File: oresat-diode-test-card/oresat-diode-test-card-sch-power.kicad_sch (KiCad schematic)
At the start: 90 parts, among them Q1 DMP2240UDM, Q2 DMP3050LVT-7, Q7 MOSFET-PCH-SOT23-6, Q8 PMV45EN, Q9 PMV45EN, U10 TPS62111RSA, U11 MIC842LYC5, U12 MIC842LYC5, U2 MAX7310, U3 TS5A21366DCUR, U6 MAX4211

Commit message: Quick design review on schematic; basically ready for layout.
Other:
- title: OreSat M0 Proto Card: Power -> OreSat Diode Test Card
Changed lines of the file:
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@@
 	(paper "USLedger")
 	(title_block
-		(title "OreSat M0 Proto Card: Power")
-		(date "2024-03-21")
-		(rev "5.0")
+		(title "OreSat Diode Test Card")
+		(date "2024-04-21")
+		(rev "v1.0")
 	)
 	(junction

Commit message: Lots of schematic cleanup - replace weird ground and power symbols with more kicad ones, fix values, fix OPD connections and address, update PCB
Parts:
- removed R6, R7: 0, oresat-passives:0603-C-NOSILK, symbol oresat-proto-card-eagle-import:R-US_0603-C-NOSILK
- added TP301: TEST-POINT-LARGE-SQUARE, oresat-proto-card:1X01, symbol oresat-proto-card-eagle-import:TEST-POINT-LARGE-SQUARE
- R1, R2: value RC0603FR-0710KL -> 2.7k
- R17: value 10k -> 2.7k
- R3: value 2.7k -> 10k
- R46, R54, R58: value NP -> 2.7k; now fitted
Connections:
- net CB_CTRL is gone; now on net CB-RESET: Q9.1 (G), R5.1, TP39.1, U6.3 (LE), U6.4 (COUT1), U6.6 (COUT2)
- net at U2.5 (IO1): now also TP301.1
- net UART_EN: now reaches U3.3 (IN2), U3.7 (IN1)
- net UART_EN: now also U2.12 (IO7)
- net at TP36.1: now also U2.4 (IO0); no longer U2.12 (IO7)
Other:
- note added: "Address selection for Card (See MAX7310 datasheet) OreSat Diode Test Card = 0x11"
- note removed: "Address selection for Card (See MAX7310 datasheet)"
- note removed: "To STM32 I2C bootloader"
- moved on the sheet: TP36, TP40

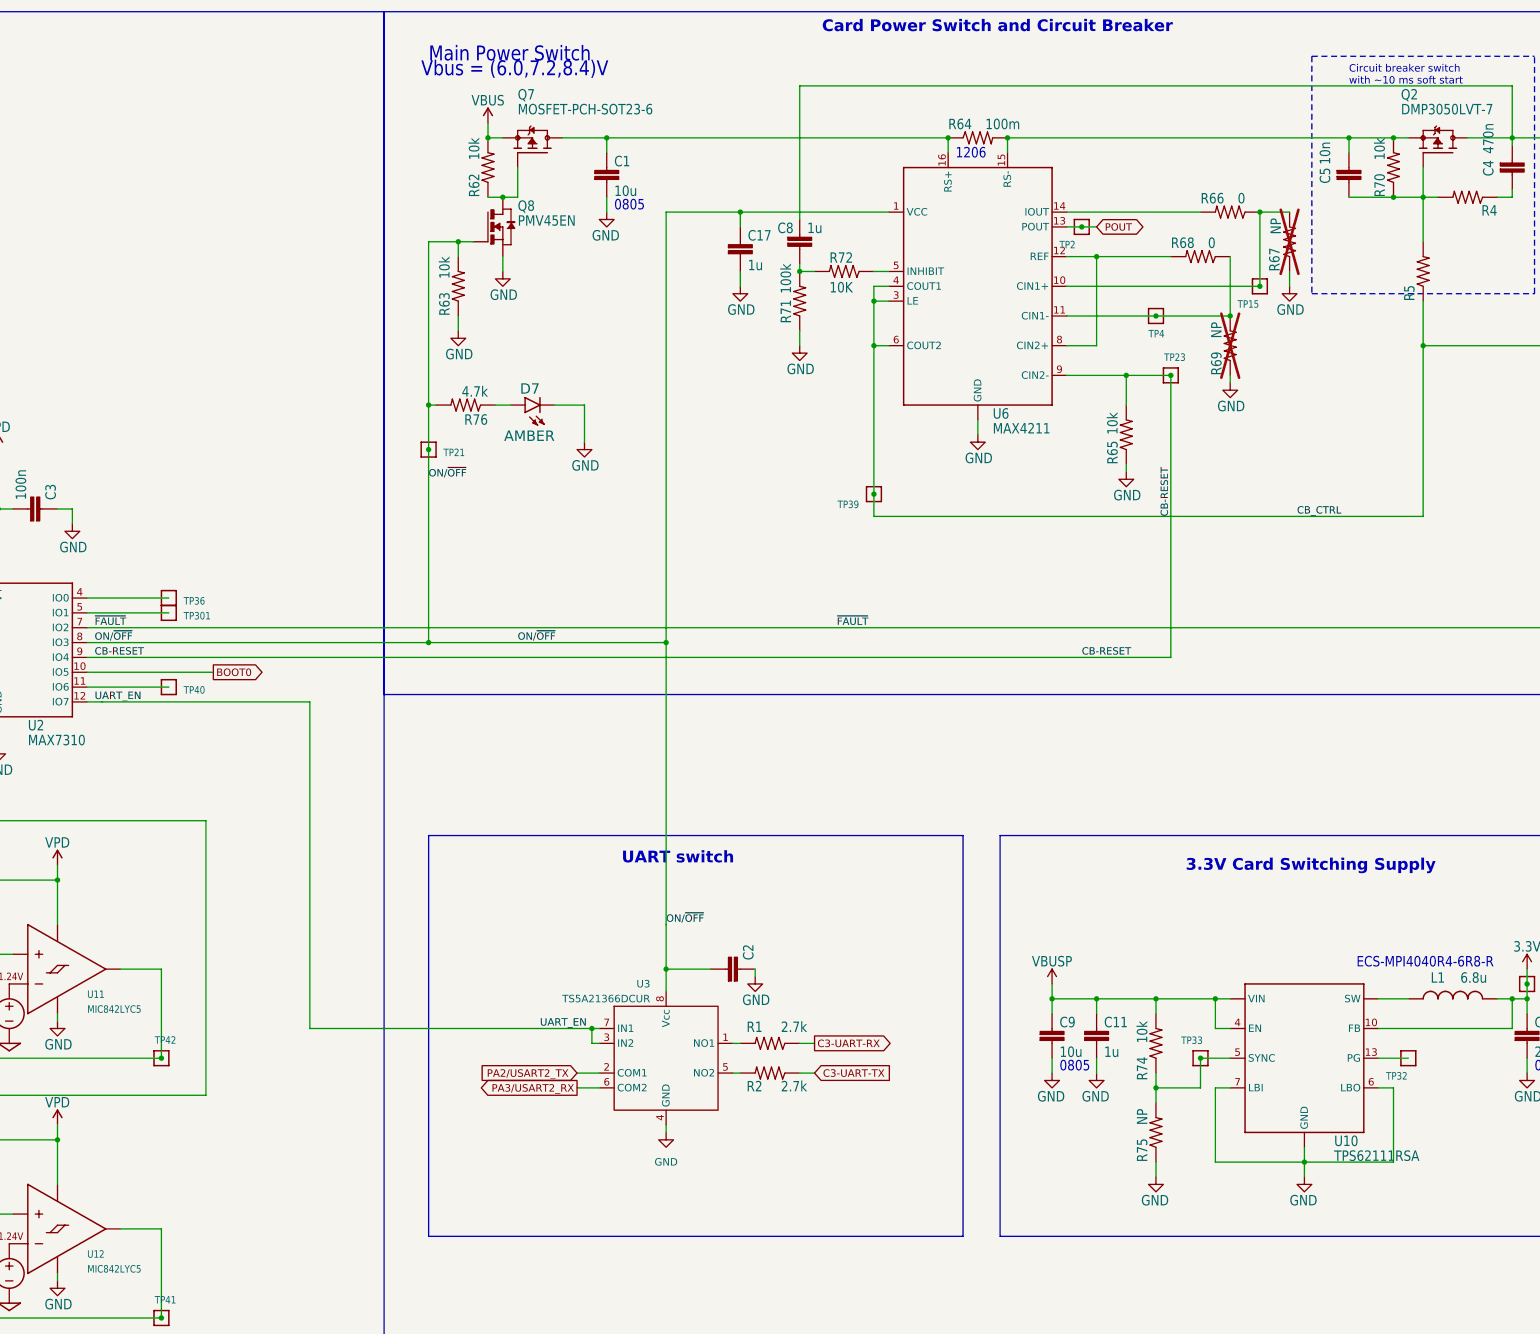
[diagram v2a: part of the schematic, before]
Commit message: Clean up of EAGLE imported ICs, added build directory, moved and locked diode hats.
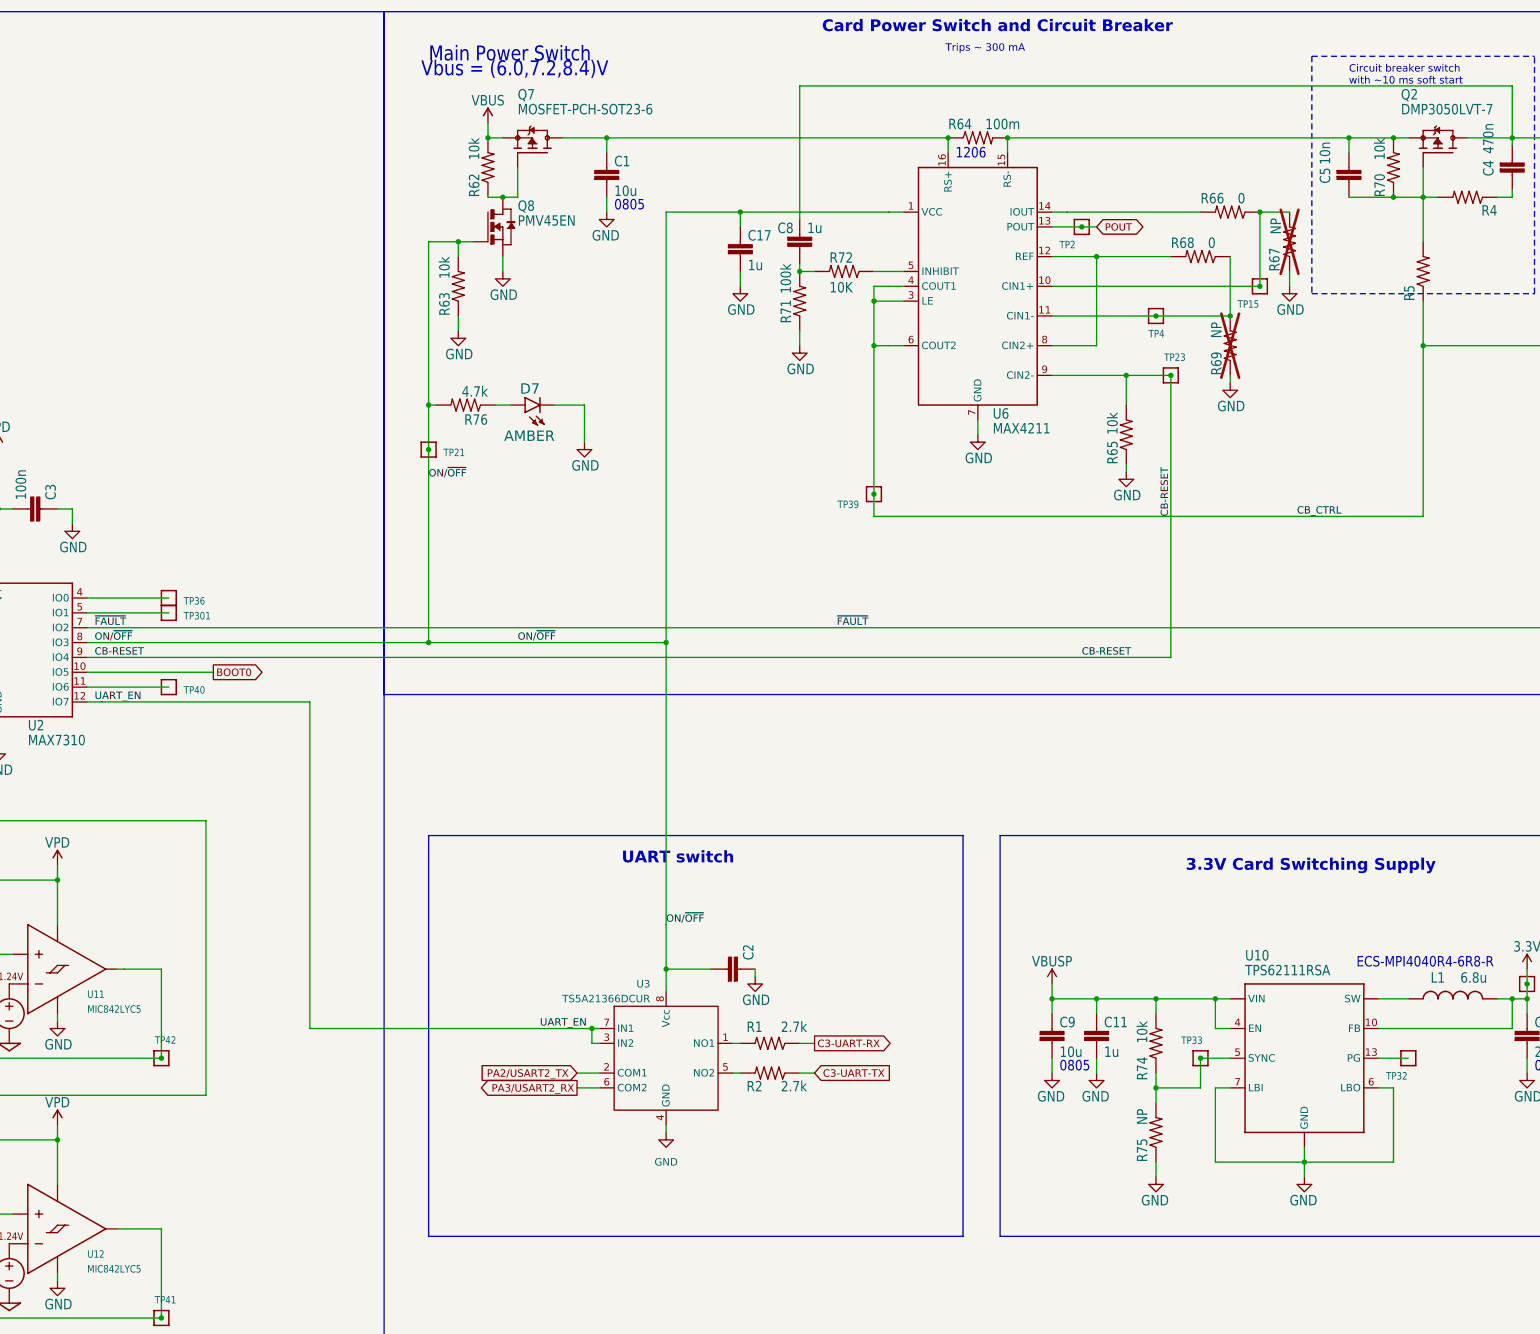
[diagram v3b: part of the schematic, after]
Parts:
- U11, U12: footprint oresat-proto-card:SC70-5 -> Package_TO_SOT_SMD:SOT-353_SC-70-5; symbol oresat-proto-card-eagle-import:MIC842LYC5 -> oresat-ics:MIC842LYC5
- U6: footprint oresat-proto-card:QFN65P400X400X80-17T210 -> Package_DFN_QFN:QFN-16-1EP_4x4mm_P0.65mm_EP2.1x2.1mm; symbol oresat-proto-card-eagle-import:MAX4211 -> oresat-ics:MAX4211FETE
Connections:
- net GND: now also U6.17 (GND); no longer U6.EPAD (GND)
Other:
- note added: "Trips ~ 300 mA"
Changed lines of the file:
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@@
 	(wire
 		(pts
-			(xy 302.26 52.07) (xy 304.8 52.07)
-		)
-		(stroke
-			(width 0.1524)
-			(type solid)
-		)
-	)
-	(wire
-		(pts
 			(xy 393.7 120.65) (xy 134.62 120.65)
 		)
@@
 	(wire
 		(pts
+			(xy 139.7 223.52) (xy 147.32 223.52)
+		)
+		(stroke
+			(width 0)
+			(type default)
+		)
+	)
+	(wire
+		(pts
 			(xy 208.28 46.99) (xy 208.28 41.91)
 		)
@@
 	(wire
 		(pts
-			(xy 269.24 64.77) (xy 271.78 64.77)
+			(xy 269.24 64.77) (xy 274.32 64.77)
 		)
 		(stroke
@@
 	(wire
 		(pts
+			(xy 299.72 57.15) (xy 302.26 57.15)
+		)
+		(stroke
+			(width 0)
+			(type default)
+		)
+	)
+	(wire
+		(pts
 			(xy 342.9 214.63) (xy 342.9 212.09)
 		)
@@
 	(wire
 		(pts
+			(xy 139.7 179.07) (xy 140.97 179.07)
+		)
+		(stroke
+			(width 0)
+			(type default)
+		)
+	)
+	(wire
+		(pts
 			(xy 96.52 208.28) (xy 96.52 220.98)
 		)
@@
 	(wire
 		(pts
+			(xy 140.97 179.07) (xy 147.32 179.07)
+		)
+		(stroke
+			(width 0.1524)
+			(type solid)
+		)
+	)
+	(wire
+		(pts
 			(xy 271.78 62.23) (xy 269.24 62.23)
 		)
@@
 	(wire
 		(pts
+			(xy 271.78 49.53) (xy 274.32 49.53)
+		)
+		(stroke
+			(width 0)
+			(type default)
+		)
+	)
+	(wire
+		(pts
 			(xy 93.98 69.85) (xy 93.98 72.39)
 		)
@@
 	(wire
 		(pts
+			(xy 271.78 62.23) (xy 274.32 62.23)
+		)
+		(stroke
+			(width 0)
+			(type default)
+		)
+	)
+	(wire
+		(pts
 			(xy 114.3 165.1) (xy 114.3 163.83)
 		)
@@
 	(wire
 		(pts
-			(xy 317.5 67.31) (xy 302.26 67.31)
-		)
-		(stroke
-			(width 0.1524)
-			(type solid)
-		)
-	)
-	(wire
-		(pts
 			(xy 45.72 67.31) (xy 58.42 67.31)
 		)
@@
 	(wire
 		(pts
+			(xy 299.72 62.23) (xy 335.28 62.23)
+		)
+		(stroke
+			(width 0.1524)
+			(type solid)
+		)
+	)
+	(wire
+		(pts
 			(xy 198.12 54.61) (xy 193.04 54.61)
 		)
@@
 	(wire
 		(pts
-			(xy 271.78 59.69) (xy 269.24 59.69)
+			(xy 269.24 59.69) (xy 274.32 59.69)
 		)
 		(stroke
@@
 	(wire
 		(pts
-			(xy 312.42 77.47) (xy 302.26 77.47)
+			(xy 45.72 125.73) (xy 45.72 67.31)
 		)
 		(stroke
@@
 	(wire
 		(pts
-			(xy 45.72 125.73) (xy 45.72 67.31)
+			(xy 91.44 125.73) (xy 104.14 125.73)
 		)
 		(stroke
@@
 	(wire
 		(pts
-			(xy 91.44 125.73) (xy 104.14 125.73)
+			(xy 299.72 72.39) (xy 307.34 72.39)
 		)
 		(stroke
@@
 	(wire
 		(pts
-			(xy 302.26 62.23) (xy 335.28 62.23)
+			(xy 299.72 67.31) (xy 317.5 67.31)
 		)
 		(stroke
@@
 	(wire
 		(pts
+			(xy 299.72 52.07) (xy 304.8 52.07)
+		)
+		(stroke
+			(width 0.1524)
+			(type solid)
+		)
+	)
+	(wire
+		(pts
 			(xy 218.44 196.85) (xy 222.25 196.85)
 		)
@@
 	(wire
 		(pts
+			(xy 271.78 72.39) (xy 274.32 72.39)
+		)
+		(stroke
+			(width 0)
+			(type default)
+		)
+	)
+	(wire
+		(pts
 			(xy 403.86 31.75) (xy 403.86 36.83)
 		)
@@
 	(wire
 		(pts
-			(xy 381 186.69) (xy 381 184.15)
+			(xy 299.72 49.53) (xy 302.26 49.53)
 		)
 		(stroke
-			(width 0.1524)
-			(type solid)
+			(width 0)
+			(type default)
 		)
 	)
 	(wire
 		(pts
-			(xy 140.335 179.07) (xy 147.32 179.07)
+			(xy 381 186.69) (xy 381 184.15)
 		)
 		(stroke
@@
 	(wire
 		(pts
-			(xy 140.335 223.52) (xy 147.32 223.52)
-		)
-		(stroke
-			(width 0.1524)
-			(type solid)
-		)
-	)
-	(wire
-		(pts
 			(xy 137.16 133.35) (xy 134.62 133.35)
 		)
@@
 	(wire
 		(pts
-			(xy 302.26 72.39) (xy 307.34 72.39)
+			(xy 299.72 77.47) (xy 312.42 77.47)
 		)
 		(stroke
@@
 		)
 	)
+	(text "Trips ~ 300 mA"
+		(exclude_from_sim no)
+		(at 288.29 21.59 0)
+		(effects
+			(font
+				(size 1.27 1.27)
+			)
+		)
+	)
 	(text "Note: Address 0b0111110x is\nreserved on all oresat cards"
 		(exclude_from_sim no)
@@
 	)
 	(symbol
-		(lib_id "oresat-proto-card-eagle-import:MIC842LYC5")
+		(lib_id "oresat-ics:MIC842LYC5")
 		(at 129.54 179.07 0)
 		(unit 1)
@@
 			)
 		)
-		(property "Footprint" "oresat-proto-card:SC70-5"
+		(property "Footprint" "Package_TO_SOT_SMD:SOT-353_SC-70-5"
 			(at 129.54 179.07 0)
 			(effects
@@
 			)
 		)
-		(property "Datasheet" ""
+		(property "Datasheet" "https://ww1.microchip.com/downloads/aemDocuments/documents/OTH/ProductDocuments/DataSheets/20005758A.pdf"
 			(at 129.54 179.07 0)
 			(effects
@@
 			)
 		)
-		(property "Description" ""
+		(property "Description" "IC Single Comparator W/REF, SC-70-5"
 			(at 129.54 179.07 0)
 			(effects
@@
 		(pin "4"
 		)
+		(pin "3"
+		)
 		(instances
 			(project "oresat-diode-test-card"
@@
 		(dnp no)
 		(property "Reference" "U10"
-			(at 347.98 209.55 0)
+			(at 332.74 177.8 0)
 			(effects
 				(font
@@
 		)
 		(property "Value" "TPS62111RSA"
-			(at 347.98 212.09 0)
+			(at 332.74 180.34 0)
 			(effects
 				(font
@@
 	)
 	(symbol
-		(lib_id "oresat-proto-card-eagle-import:MAX4211")
+		(lib_id "oresat-ics:MAX4211FETE")
 		(at 287.02 59.69 0)
 		(unit 1)
@@
 			)
 		)
-		(property "Footprint" "oresat-proto-card:QFN65P400X400X80-17T210"
-			(at 287.02 59.69 0)
+		(property "Footprint" "Package_DFN_QFN:QFN-16-1EP_4x4mm_P0.65mm_EP2.1x2.1mm"
+			(at 271.78 44.45 0)
 			(effects
 				(font
@@
 			)
 		)
-		(property "Datasheet" ""
-			(at 287.02 59.69 0)
+		(property "Datasheet" "https://www.mouser.com/datasheet/2/256/MAX4210-MAX4211-1265251.pdf"
+			(at 271.78 44.45 0)
 			(effects
 				(font
@@
 			)
 		)
-		(property "Description" ""
+		(property "Description" "IC Current monitor, 16-TQFN"
 			(at 287.02 59.69 0)
 			(effects
@@
 		(pin "8"
 		)
-		(pin "EPAD"
+		(pin "17"
+		)
+		(pin "2"
 		)
 		(instances
@@
 	)
 	(symbol
-		(lib_id "oresat-proto-card-eagle-import:MIC842LYC5")
+		(lib_id "oresat-ics:MIC842LYC5")
 		(at 129.54 223.52 0)
 		(unit 1)
@@
 			)
 		)
-		(property "Footprint" "oresat-proto-card:SC70-5"
+		(property "Footprint" "Package_TO_SOT_SMD:SOT-353_SC-70-5"
 			(at 129.54 223.52 0)
 			(effects
@@
 			)
 		)
-		(property "Datasheet" ""
+		(property "Datasheet" "https://ww1.microchip.com/downloads/aemDocuments/documents/OTH/ProductDocuments/DataSheets/20005758A.pdf"
 			(at 129.54 223.52 0)
 			(effects
@@
 			)
 		)
-		(property "Description" ""
+		(property "Description" "IC Single Comparator W/REF, SC-70-5"
 			(at 129.54 223.52 0)
 			(effects
@@
 		(pin "2"
 		)
+		(pin "3"
+		)
 		(instances

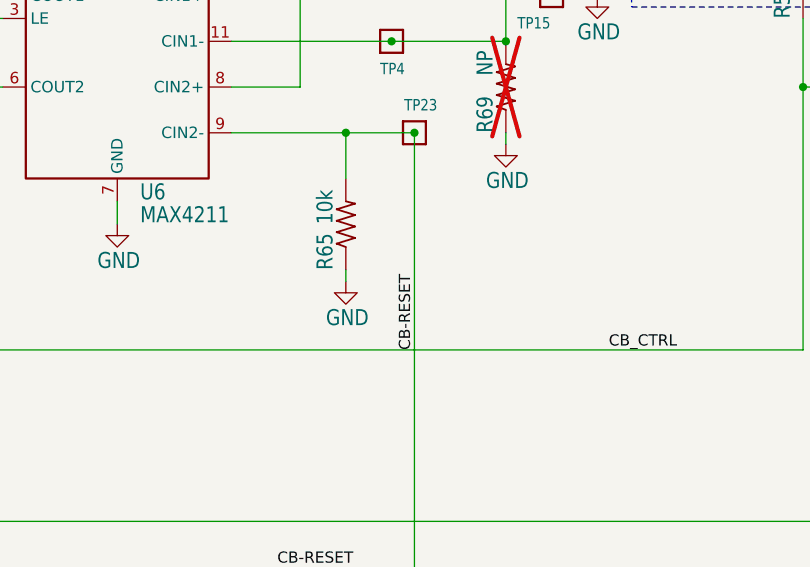
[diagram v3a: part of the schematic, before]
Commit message: Fix OPD weirdness, lots of little polishing including power plane movement and thicker traces.
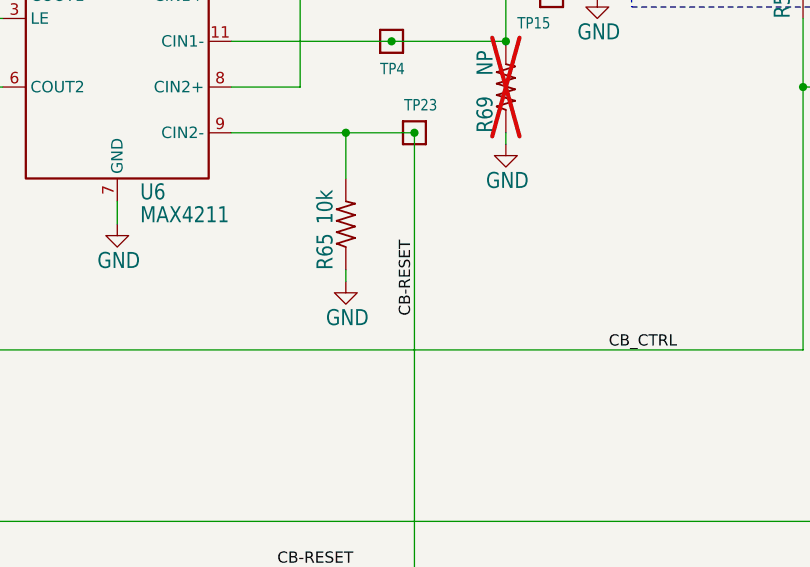
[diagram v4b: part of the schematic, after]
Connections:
- net CB-RESET: no longer Q9.1 (G), R5.1, TP39.1, U6.3 (LE), U6.4 (COUT1), U6.6 (COUT2)
- new net CB_CTRL: Q9.1 (G), R5.1, TP39.1, U6.3 (LE), U6.4 (COUT1), U6.6 (COUT2)
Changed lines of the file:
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@@
 	)
 	(label "CB-RESET"
-		(at 320.04 101.6 90)
+		(at 320.04 97.79 90)
 		(fields_autoplaced yes)
 		(effects

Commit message: Added BOM
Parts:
- C1, C11, C16, C17, C22, C23, C3, C9, D3, D6, D7, L1, Q1, Q2, Q7, Q8, Q9, R17, R24, R3, R39, R40, R45, R46, R52, R53, R54, R55, R56, R57, R58, R59, R60, R61, R62, R63, R64, R65, R66, R67, R68, R69, R70, R71, R72, R73, R74, R75, R76, R77, R78, R79, R80, R81, R82, R83, U10, U2, U6: DST (none) -> Digi-Key
- U3: DPN (none) -> 296-24304-1-ND; DST (none) -> Digi-Key; MFR (none) -> Texas Instruments; MPN (none) -> TS5A21366DCUR
